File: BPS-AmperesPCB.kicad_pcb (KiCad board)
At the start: 2 copper layers, 40 parts, among them J1 Conn_01x04, J2 PeripheralCANConnector, J3 PeripheralCANConnector, U1 PeripheralSOM, U2 INA145UA/2K5, U3 AMC1300BDWV, U4 RO-123.3S_HP

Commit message: tag team
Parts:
- added D4: PowerOn, LED_SMD:LED_0805_2012Metric, F.Cu at (115.5, 47.2)
- added R9: 1.5k, Resistor_SMD:R_0805_2012Metric, F.Cu at (115.5, 50.8)
- U1: moved to F.Cu
- moved GND1 168.0 mm to (103.2, 39.6)
- moved OUTP1 165.0 mm to (121.1, 86.8)
- moved GNDHigh1 160.7 mm to (112.0, 39.6)
- moved INN1 146.9 mm to (129.4, 39.6)
- moved VOut1 146.9 mm to (138.3, 86.8)
- moved +3V3 145.5 mm to (120.7, 39.6)
- moved D1 144.3 mm to (110.5, 47.2), turned to -90 degrees
- moved GNDPWR1 140.6 mm to (112.5, 86.8)
- moved INP1 139.7 mm to (138.1, 39.6)
- moved R5 137.3 mm to (110.5, 50.8), turned to 90 degrees
- moved +12V1 132.9 mm to (103.2, 86.8)
- moved OUTN1 131.8 mm to (129.7, 86.8)
- moved +3V3High1 121.0 mm to (146.8, 39.6)
- moved ADC_In1 100.0 mm to (146.8, 86.8)
- moved U1 25.6 mm to (121.9, 64.4)
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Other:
- board text added: "+3V3"
- board text added: "+3V3 High"

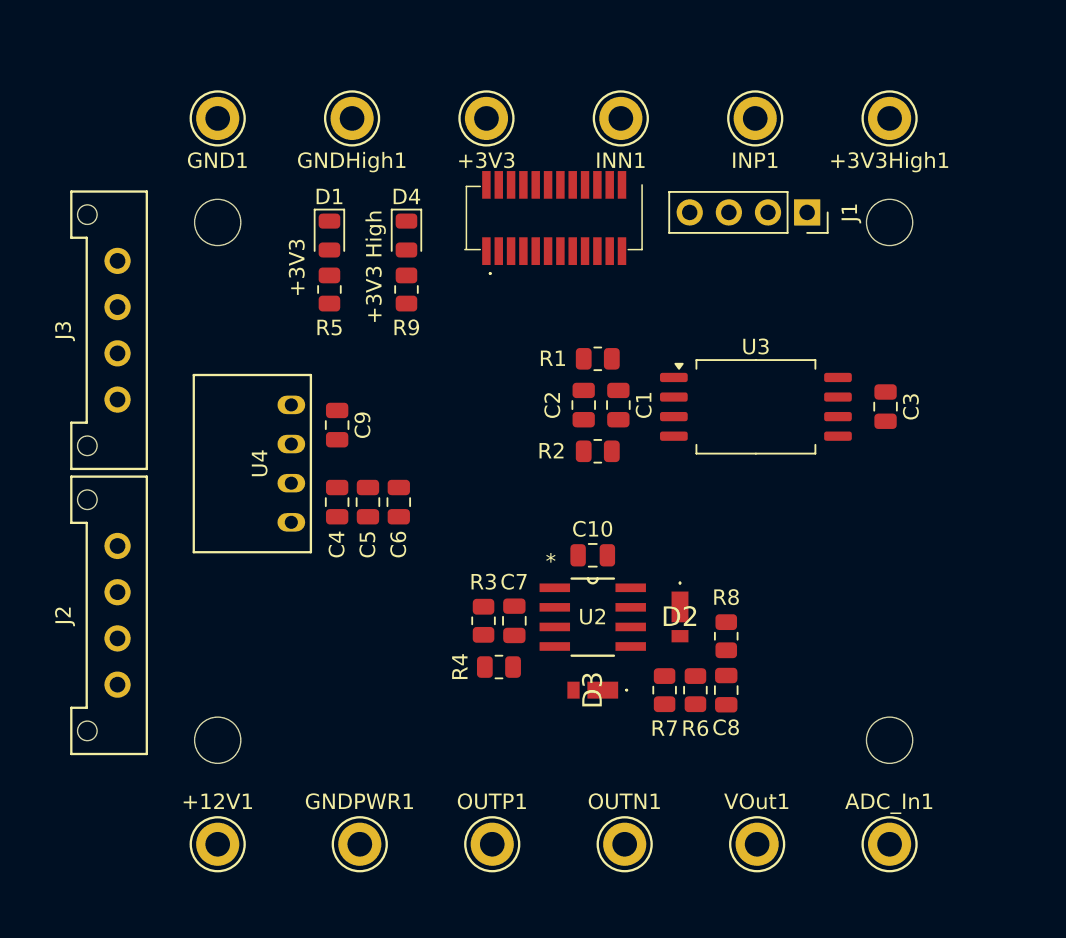
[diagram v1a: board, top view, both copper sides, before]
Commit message: changed layout
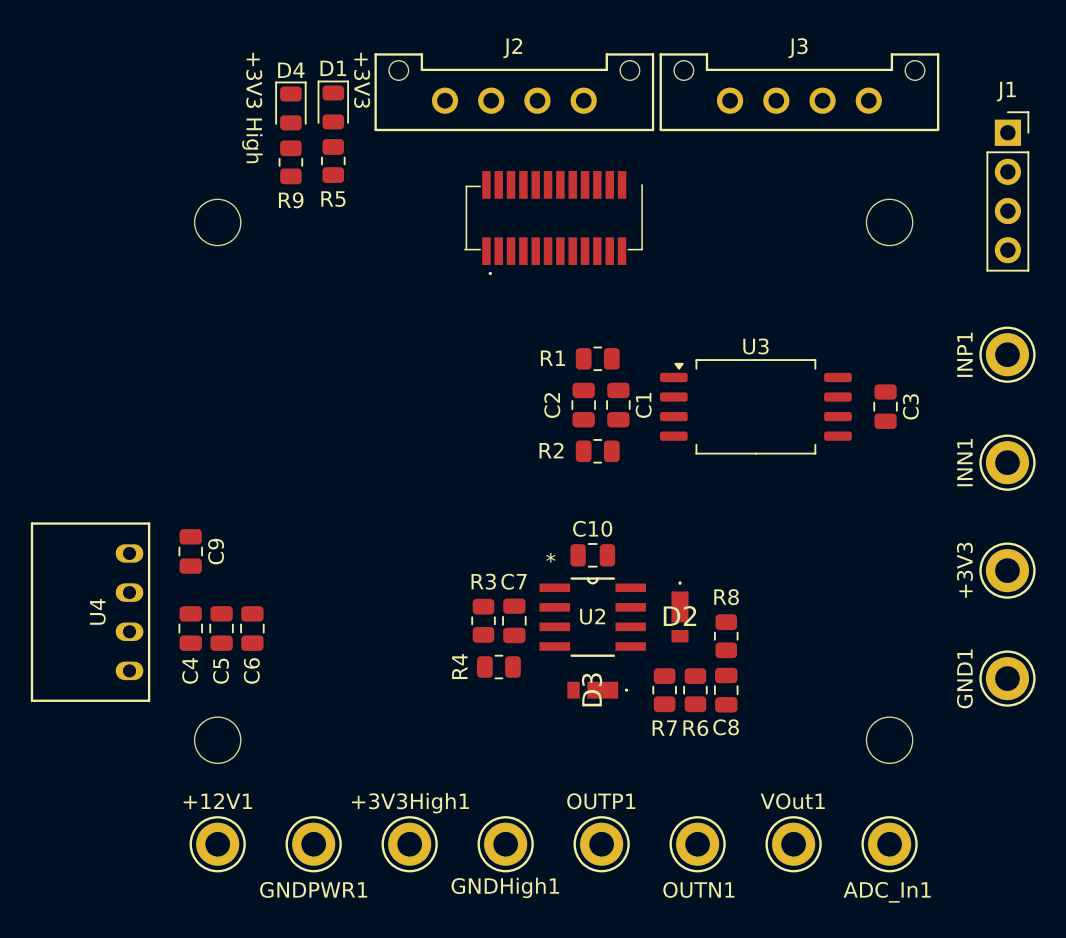
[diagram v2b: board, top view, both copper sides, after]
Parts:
- moved GND1 62.8 mm to (154.5, 76.0), turned to 90 degrees
- moved +3V3High1 56.5 mm to (115.7, 86.8)
- moved GNDHigh1 48.1 mm to (121.9, 86.8)
- moved +3V3 44.8 mm to (154.5, 69.0), turned to 90 degrees
- moved J3 44.2 mm to (136.5, 38.5), turned to 0 degrees
- moved J2 43.4 mm to (118.0, 38.5), turned to 0 degrees
- moved INN1 33.6 mm to (154.5, 62.0), turned to 90 degrees
- moved INP1 22.4 mm to (154.5, 55.0), turned to 90 degrees
- moved U4 14.3 mm to (97.5, 71.7)
- moved J1 14.0 mm to (154.5, 40.6), turned to 0 degrees
- moved C4 12.5 mm to (101.5, 72.8)
- moved C5 12.5 mm to (103.5, 72.8)
- moved C6 12.5 mm to (105.5, 72.8)
- moved C9 12.5 mm to (101.5, 67.8)
- moved D4 11.1 mm to (108.0, 39.0)
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
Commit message: reviewable
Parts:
- moved +3V3 80.2 mm to (74.8, 60.0)
- moved GND1 79.3 mm to (75.8, 85.6)
- moved OUTN1 60.4 mm to (75.0, 76.0)
- moved OUTP1 57.0 mm to (74.8, 66.8)
- moved VOut1 54.3 mm to (86.3, 87.2), turned to 180 degrees
- moved GNDPWR1 53.9 mm to (133.2, 38.4), turned to 90 degrees
- moved +12V1 52.1 mm to (133.6, 44.4), turned to 90 degrees
- moved ADC_In1 49.3 mm to (97.6, 86.8), turned to 90 degrees
- moved C3 49.0 mm to (97.6, 57.9), turned to 90 degrees
- moved +3V3High1 41.9 mm to (134.6, 49.4)
- moved U4 39.7 mm to (122.6, 40.9), turned to 0 degrees
- moved J2 38.6 mm to (79.4, 38.6)
- moved C10 37.7 mm to (89.9, 65.8)
- moved C7 37.7 mm to (84.8, 70.0)
- moved C8 37.7 mm to (98.6, 74.5)
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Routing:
- net +12V: track 0.00 -> 77.5 mm
- net GNDPWR: track 0.00 -> 73.0 mm
- net +3V3: track 0.00 -> 57.1 mm
- net GND High: track 0.00 -> 56.7 mm, vias 0 -> 2
- net +3V3 High: track 0.00 -> 56.3 mm, vias 0 -> 1
- net /ADC_In: track 0.00 -> 52.6 mm, vias 0 -> 2
- net /OUTN: track 0.00 -> 44.5 mm, vias 0 -> 2
- net /OUTP: track 0.00 -> 41.3 mm, vias 0 -> 2
- net Net-(J2-CAN_L): track 0.00 -> 40.3 mm
- net Net-(J2-CAN_H): track 0.00 -> 35.2 mm
- net /INP: track 0.00 -> 33.5 mm
- net Net-(D2-A): track 0.00 -> 30.0 mm
- net /INN: track 0.00 -> 28.7 mm
- net Net-(J1-Pin_1): track 0.00 -> 16.9 mm, vias 0 -> 1
- net Net-(U2-RG): track 0.00 -> 5.75 mm
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- added copper zone on F.Cu, net +3V3
- added copper zone on B.Cu, net /MISO
- added copper zone on F.Cu, net /MISO
- added copper zone on B.Cu, net GND
- added copper zone on F.Cu, net GND
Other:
- board outline added: 70 x 58 mm

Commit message: reviewable part 2
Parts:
- moved GNDHigh1 33.4 mm to (123.5, 88.6), turned to 0 degrees
- moved D4 18.3 mm to (128.4, 69.9)
- moved R9 15.8 mm to (128.4, 67.2), turned to 180 degrees
- moved INP1 12.6 mm to (133.5, 88.6), turned to 180 degrees
- moved +3V3High1 9.27 mm to (133.5, 58.6)
- moved J1 9.18 mm to (134.5, 72.4)
- moved INN1 8.13 mm to (133.5, 78.6), turned to 180 degrees
- moved ADC_In1 4.48 mm to (93.5, 88.6), turned to 0 degrees
- moved +12V1 4.20 mm to (133.6, 48.6), turned to 0 degrees
- moved GND1 3.78 mm to (73.5, 88.6), turned to 180 degrees
- moved J2 3.70 mm to (83.1, 38.8)
- moved VOut1 3.11 mm to (83.5, 88.6)
- moved C3 3.01 mm to (97.4, 60.9), turned to -90 degrees
- moved OUTN1 3.00 mm to (73.5, 78.6), turned to 180 degrees
- moved OUTP1 2.22 mm to (73.5, 68.6)
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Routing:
- net GNDPWR: track 73.0 -> 0.00 mm
- net GND High: track 56.7 -> 9.02 mm, vias 2 -> 0
- net +3V3: track 57.1 -> 86.9 mm
- net /INP: track 33.5 -> 51.9 mm
- net +3V3 High: track 56.3 -> 68.8 mm
- net /INN: track 28.7 -> 39.3 mm
- net /OUTP: track 41.3 -> 33.0 mm, vias 2 -> 0
- net Net-(J1-Pin_1): track 16.9 -> 24.0 mm
- net Net-(J2-CAN_L): track 40.3 -> 34.3 mm
- net Net-(J2-CAN_H): track 35.2 -> 40.1 mm
- net GND: track 3.30 -> 6.65 mm, vias 1 -> 0
- net Net-(D2-A): track 30.0 -> 33.3 mm
- net Net-(D4-A): track 0.00 -> 2.71 mm
- net /OUTN: track 44.5 -> 46.4 mm
- net +12V: track 77.5 -> 76.0 mm
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- added copper zone on B.Cu, net GND High
- added copper zone on F.Cu, net GND High
- added copper zone on B.Cu, net GNDPWR
- added copper zone on F.Cu, net GNDPWR
- removed copper zone on F.Cu, net +3V3
- removed copper zone on B.Cu, net /MISO
- removed copper zone on F.Cu, net /MISO
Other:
- board size 70 x 58 mm -> 70 x 60 mm

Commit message: decor fancy
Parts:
- added LOGO1: aniMegamind, Parts:aniMegamind, B.Cu at (114.4, 69.0)
- added LOGO2: aniMegamind, UTSVT_Special:UTSVT_Logo_Symbol, B.Cu at (95.3, 73.9)
- moved C9 2.27 mm to (120.3, 47.6)
- moved R2 0.65 mm to (116.9, 54.5)
- moved C8 0.28 mm to (98.9, 74.7)
- moved R8 0.28 mm to (98.9, 71.2)
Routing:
- net GND High: track 9.02 -> 0.00 mm
- net Net-(J1-Pin_1): track 24.0 -> 28.4 mm
- net /INP: track 51.9 -> 47.5 mm
- net +12V: track 76.0 -> 80.0 mm
- net /ADC_In: track 54.1 -> 50.3 mm
- net Net-(J2-CAN_H): track 40.1 -> 41.4 mm
- net GND: track 6.65 -> 7.82 mm
- net Net-(J2-CAN_L): track 34.3 -> 35.2 mm
- net +3V3 High: track 68.8 -> 69.5 mm
- net /INN: track 39.3 -> 40.0 mm
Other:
- board text added: "LHR Solar Amperes Board By: Nathan and Aniruddh"

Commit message: tada
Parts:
- LOGO2: value aniMegamind -> solarlogo
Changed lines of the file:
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@@
 		(fp_arc
 			(start 18.037742 -21.812258)
-			(mid 20.300485 -20.874999)
+			(mid 20.300482 -20.874999)
 			(end 21.237742 -18.612258)
 			(stroke
@@
 			)
 		)
-		(property "Value" "aniMegamind"
+		(property "Value" "solarlogo"
 			(at 0.75 0 0)
 			(layer "B.SilkS")

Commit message: bored so i did lhr
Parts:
- removed +3V3High1, ADC_In1, GNDHigh1: TestPoint, TestPoint:TestPoint_Keystone_5005-5009_Compact
- added +3V3H1: TestPoint, TestPoint:TestPoint_Keystone_5005-5009_Compact, F.Cu at (133.5, 58.6)
- added GNDH1: TestPoint, TestPoint:TestPoint_Keystone_5005-5009_Compact, F.Cu at (123.5, 88.6)
- added aOut1: TestPoint, TestPoint:TestPoint_Keystone_5005-5009_Compact, F.Cu at (103.5, 88.6)
- moved D4 17.6 mm to (131.7, 52.6)
- moved R9 16.7 mm to (129.8, 50.6), turned to 0 degrees
- moved GND1 10.0 mm to (83.5, 88.6)
- moved OUTP1 10.0 mm to (73.5, 78.6)
- moved VOut1 10.0 mm to (93.5, 88.6)
- moved +3V3 10.00 mm to (73.5, 68.6)
- moved D1 9.56 mm to (73.5, 56.9)
- moved R5 9.56 mm to (73.5, 59.6)
- moved OUTN1 9.06 mm to (74.5, 87.6)
- moved C10 4.70 mm to (94.6, 65.4)
- moved R4 4.28 mm to (80.8, 70.2), turned to 90 degrees
- moved J1 3.60 mm to (130.9, 72.5)
- moved C3 2.75 mm to (94.7, 61.4), turned to 180 degrees
- moved INP1 1.41 mm to (132.5, 87.6)
- moved GNDPWR1 1.00 mm to (132.5, 38.6)
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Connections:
- net /ADC_In renamed /aOut
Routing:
- net +3V3 High: track 69.5 -> 59.6 mm, vias 1 -> 2
- net +12V: track 80.0 -> 71.4 mm, vias 0 -> 1
- net Net-(J1-Pin_1): track 28.4 -> 20.4 mm
- net Net-(J2-CAN_H): track 41.4 -> 36.2 mm
- net /OUTP: track 32.5 -> 36.0 mm, vias 0 -> 1
- net Net-(J2-CAN_L): track 35.2 -> 38.0 mm
- net /aOut: track 50.3 -> 52.9 mm
- net Net-(U2-V+IN): track 4.94 -> 7.58 mm
- net Net-(D2-A): track 33.6 -> 31.0 mm
- net /OUTN: track 46.4 -> 45.5 mm, vias 2 -> 0
- net Net-(D4-A): track 2.71 -> 2.02 mm
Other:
- board text added: "+12V"
- board text added: "CAN_H"
- board text added: "CAN_L"
- board text added: "GND"
- board text added: "GND GND GND GND GND"
- board text added: "GND GND GND GND GND GND"
- board text added: "GND GND GND GND GND GND GND GND GND"
- board text added: "GND High"
- board text added: "GND High GND High GND High GND High"
- board text added: "GND High GND High GND High GND High GND High"
- board text added: "GND High GND High GND High GND High GND High GND High GND High"
- board text added: "GNDPWR"
- board text added: "GNDPWR GNDPWR GNDPWR GNDPWR"
- board text added: "GNDPWR GNDPWR GNDPWR GNDPWR GNDPWR GNDPWR GNDPWR GNDPWR GNDPWR"
- board text added: "IN N"
- board text added: "IN P"
- board text added: "LHR Solar: Amperes Board By: Nathan and Aniruddh"
- board text added: "OUT N"
- board text added: "OUT P"
- board text added: "SHUNT"
- board text added: "VOut"
- board text added: "aOut"
- board text removed: "LHR Solar Amperes Board By: Nathan and Aniruddh"

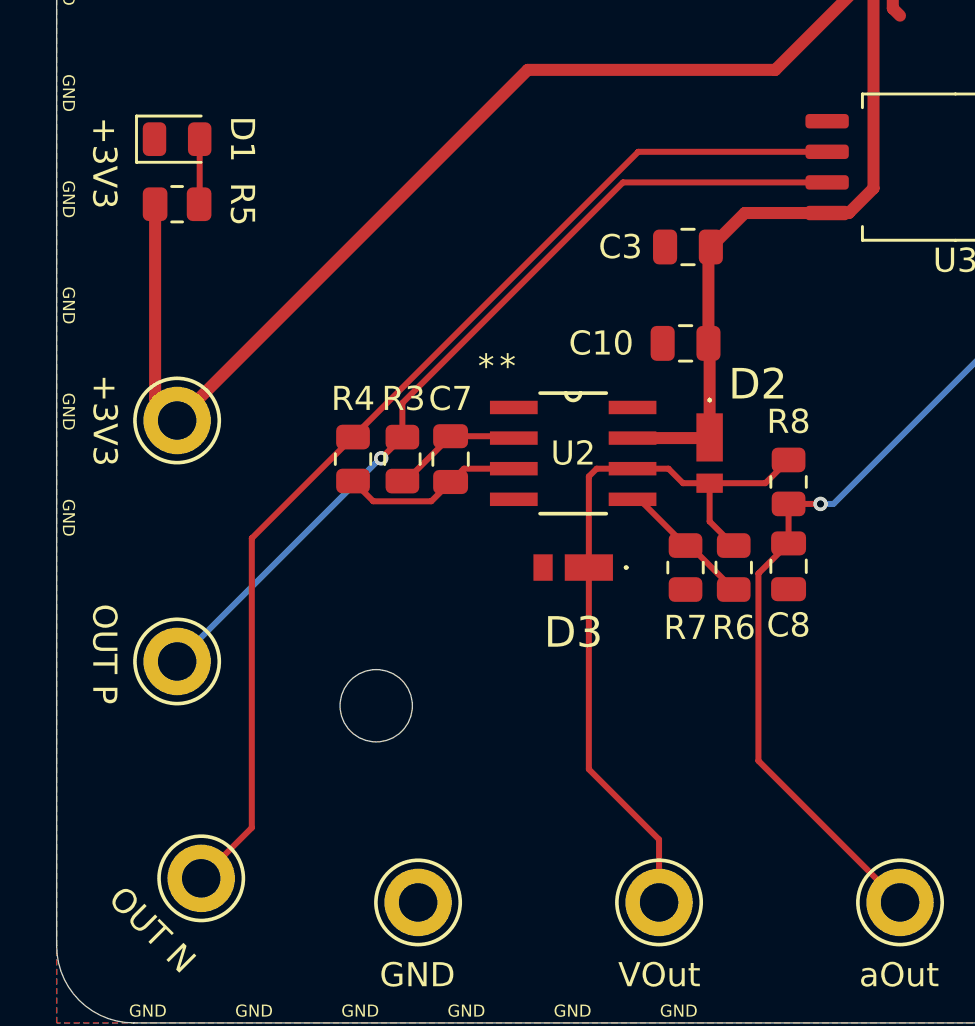
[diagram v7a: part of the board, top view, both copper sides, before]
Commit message: fixed outp and outn flip smh
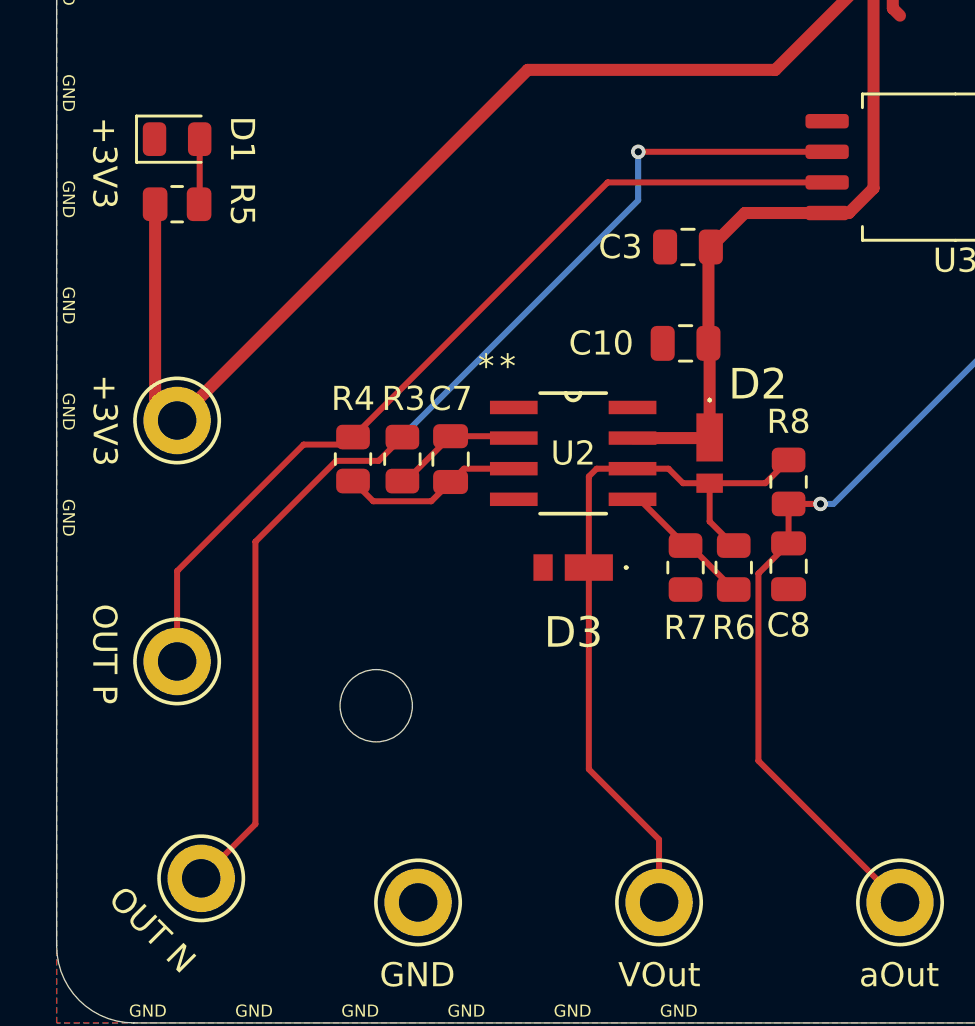
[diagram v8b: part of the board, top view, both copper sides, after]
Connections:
- R3 pad 2: /OUTP -> /OUTN
- R4 pad 2: /OUTN -> /OUTP
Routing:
- net /OUTP: track 36.0 -> 37.4 mm, vias 1 -> 0
- net /OUTN: track 45.5 -> 46.6 mm, vias 0 -> 1
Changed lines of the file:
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@@
 		)
 		(property "Value" "TestPoint"
-			(at 0 2.75 360)
+			(at 0 2.75 0)
 			(layer "F.Fab")
 			(effects
@@
 		)
 		(fp_text user "${REFERENCE}"
-			(at 0 0 360)
+			(at 0 0 0)
 			(layer "F.Fab")
 			(effects
@@
 		(tags "resistor")
 		(property "Reference" "R4"
-			(at 2.5 0 360)
+			(at 2.5 0 0)
 			(layer "F.SilkS")
 			(effects
@@
 			(layers "F.Cu" "F.Paste" "F.Mask")
 			(roundrect_rratio 0.243902)
-			(net 12 "/OUTN")
+			(net 13 "/OUTP")
 			(pintype "passive")
 		)
@@
 		(tags "Through Hole Mount Test Points")
 		(property "Reference" "OUTP1"
-			(at -3.1 0 270)
+			(at -3.1 0 -90)
 			(unlocked yes)
 			(layer "F.SilkS")
@@
 		)
 		(property "Value" "1.5k"
-			(at 0 1.65 360)
+			(at 0 1.65 0)
 			(layer "F.Fab")
 			(effects
@@
 		)
 		(fp_text user "${REFERENCE}"
-			(at 0 0 360)
+			(at 0 0 0)
 			(layer "F.Fab")
 			(effects
@@
 		(tags "Through Hole Mount Test Points")
 		(property "Reference" "OUTN1"
-			(at 2.1 -2.1 315)
+			(at 2.1 -2.1 -45)
 			(layer "F.SilkS")
 			(hide yes)
@@
 			(layers "F.Cu" "F.Paste" "F.Mask")
 			(roundrect_rratio 0.243902)
-			(net 13 "/OUTP")
+			(net 12 "/OUTN")
 			(pintype "passive")
 		)
@@
 		)
 		(property "Value" "PowerOn"
-			(at 0 1.65 360)
+			(at 0 1.65 0)
 			(layer "F.Fab")
 			(effects
@@
 		)
 		(fp_text user "${REFERENCE}"
-			(at 0 0 360)
+			(at 0 0 0)
 			(layer "F.Fab")
 			(effects
@@
 		(fp_arc
 			(start 18.037742 -21.812258)
-			(mid 20.300485 -20.874999)
+			(mid 20.300482 -20.874999)
 			(end 21.237742 -18.612258)
 			(stroke
@@
 		(tags "Through Hole Mount Test Points")
 		(property "Reference" "+3V3"
-			(at 3 0 270)
+			(at 3 0 -90)
 			(unlocked yes)
 			(layer "F.SilkS")
@@
 		)
 		(property "Value" "1uF"
-			(at 0 1.68 360)
+			(at 0 1.68 0)
 			(layer "F.Fab")
 			(effects
@@
 		)
 		(fp_text user "${REFERENCE}"
-			(at 0 0 360)
+			(at 0 0 0)
 			(layer "F.Fab")
 			(effects
@@
 	)
 	(segment
-		(start 76.6 85.5)
-		(end 76.6 73.4875)
+		(start 74.5 87.6)
+		(end 76.75 85.35)
 		(width 0.25)
 		(layer "F.Cu")
@@
 	)
 	(segment
-		(start 76.6 73.4875)
-		(end 80.8 69.2875)
+		(start 80.1049 70.275)
+		(end 81.8637 70.275)
 		(width 0.25)
 		(layer "F.Cu")
@@
 	)
 	(segment
-		(start 74.5 87.6)
-		(end 76.6 85.5)
+		(start 81.8637 70.275)
+		(end 82.84894 69.28976)
 		(width 0.25)
 		(layer "F.Cu")
@@
 	)
 	(segment
-		(start 80.8 69.2875)
-		(end 92.6375 57.45)
+		(start 76.75 85.35)
+		(end 76.75 73.6299)
+		(width 0.25)
+		(layer "F.Cu")
+		(net 12)
+	)
+	(segment
+		(start 76.75 73.6299)
+		(end 80.1049 70.275)
 		(width 0.25)
 		(layer "F.Cu")
@@
 		(net 12)
 	)
+	(via
+		(at 92.6375 57.45)
+		(size 0.6)
+		(drill 0.3)
+		(layers "F.Cu" "B.Cu")
+		(net 12)
+	)
 	(segment
-		(start 82.84894 67.874956)
-		(end 92.003896 58.72)
+		(start 92.6375 57.45)
+		(end 92.6375 59.4625)
 		(width 0.25)
-		(layer "F.Cu")
-		(net 13)
+		(layer "B.Cu")
+		(net 12)
 	)
 	(segment
-		(start 81.96935 70.16935)
-		(end 82.84894 69.28976)
+		(start 92.6375 59.4625)
+		(end 82.75 69.35)
+		(width 0.25)
+		(layer "B.Cu")
+		(net 12)
+	)
+	(segment
+		(start 100.475 58.72)
+		(end 91.3675 58.72)
 		(width 0.25)
 		(layer "F.Cu")
@@
 	)
 	(segment
-		(start 82.84894 69.28976)
-		(end 82.84894 67.874956)
+		(start 91.3675 58.72)
+		(end 80.8 69.2875)
 		(width 0.25)
 		(layer "F.Cu")
@@
 	)
 	(segment
-		(start 92.003896 58.72)
-		(end 100.475 58.72)
+		(start 80.4875 69.6)
+		(end 80.8 69.2875)
 		(width 0.25)
 		(layer "F.Cu")
 		(net 13)
 	)
-	(via
-		(at 81.96935 70.16935)
-		(size 0.6)
-		(drill 0.3)
-		(layers "F.Cu" "B.Cu")
+	(segment
+		(start 78.75 69.6)
+		(end 73.5 74.85)
+		(width 0.25)
+		(layer "F.Cu")
 		(net 13)
 	)
 	(segment
-		(start 81.96935 70.16935)
-		(end 81.93065 70.16935)
+		(start 78.75 69.6)
+		(end 80.4875 69.6)
 		(width 0.25)
-		(layer "B.Cu")
+		(layer "F.Cu")
 		(net 13)
 	)
 	(segment
-		(start 81.93065 70.16935)
+		(start 73.5 74.85)
 		(end 73.5 78.6)
 		(width 0.25)
-		(layer "B.Cu")
+		(layer "F.Cu")
 		(net 13)
 	)
